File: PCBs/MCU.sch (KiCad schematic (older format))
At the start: 21 parts, among them CON2 AVR-ISP-6, J10 SPK, U6 ATMEGA328P-AU, Y2 20Mhz

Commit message: ADX988 CAT: add FE, FI commands
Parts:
- added J7: Conn_01x10, Pin_Headers:Pin_Header_Straight_1x10_Pitch2.54mm, symbol Conn_01x10
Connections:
- net IO_0 is gone; now on net RX_TX: U6.23 ((PCINT8/ADC0)PC0)
- net +5V: now also J7.9 (Pin_9)
- net GND: now also J7.1 (Pin_1)
- net IO_4: now also J7.2 (Pin_2)
- net IO_5: now also J7.3 (Pin_3)
- net IO_6: now also J7.4 (Pin_4)
- net IO_7: now also J7.5 (Pin_5)
- net RX_TX: no longer U6.14 ((PCINT2/OC1B/~SS~)PB2)
- net ENCODER_A renamed IO_8
- net IO_8: now also J7.6 (Pin_6)
- net ENCODER_B renamed IO_9
- net IO_9: now also J7.7 (Pin_7)
- new net +12V: J7.10 (Pin_10)
- new net IO_10: J7.8 (Pin_8), U6.14 ((PCINT2/OC1B/~SS~)PB2)
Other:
- moved on the sheet: D3, D4, R12, R13

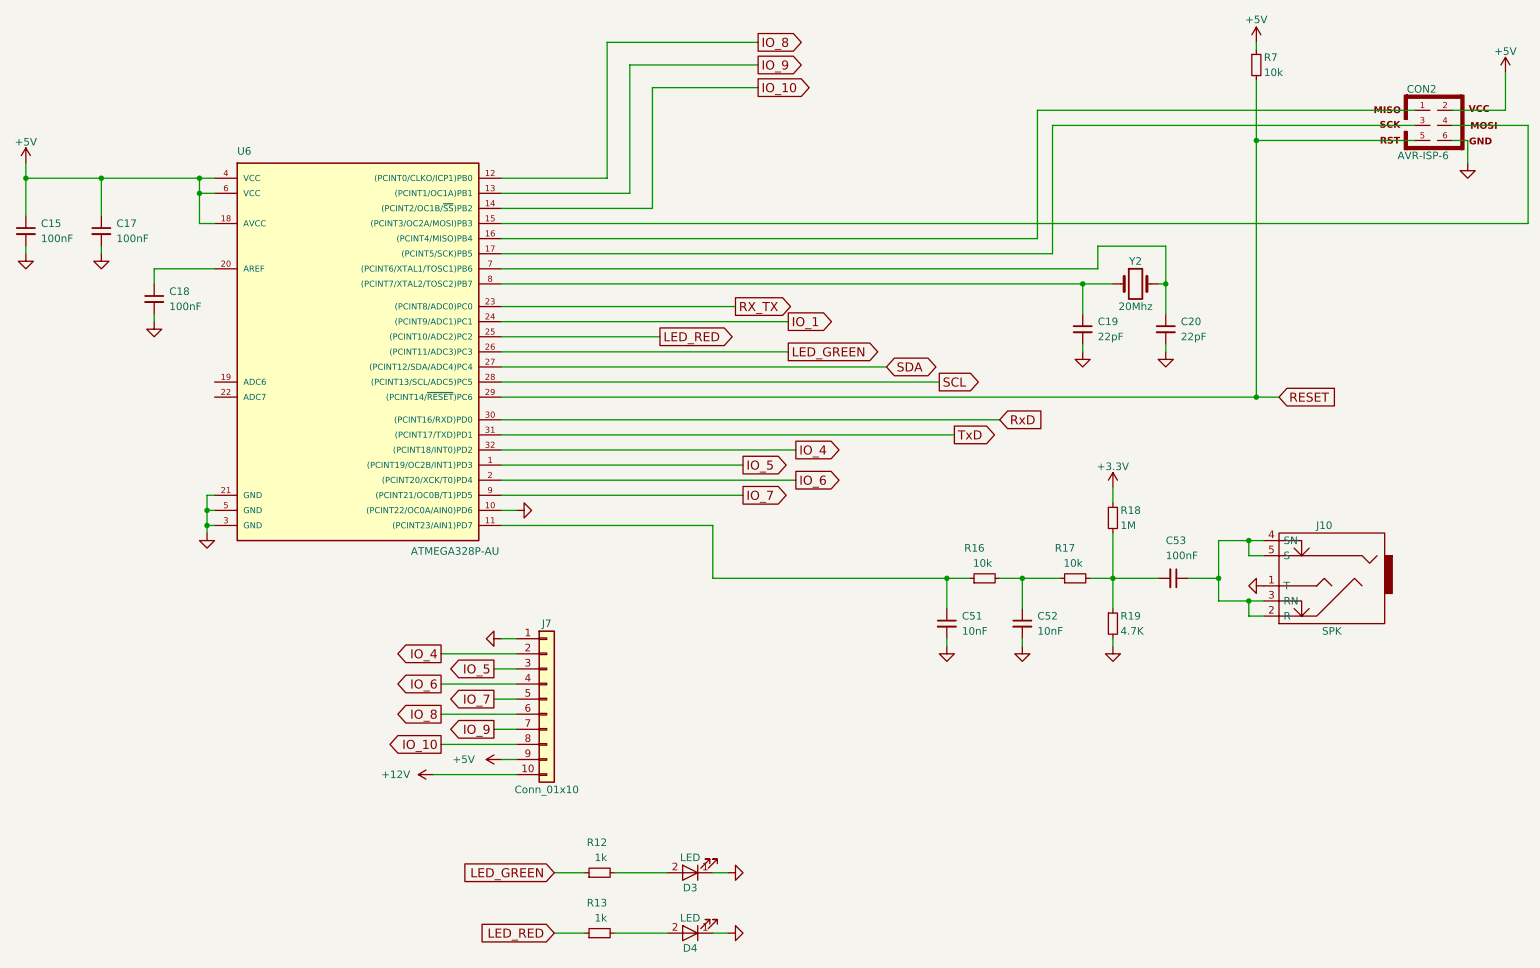
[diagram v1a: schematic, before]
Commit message: discret, simple, CH340E
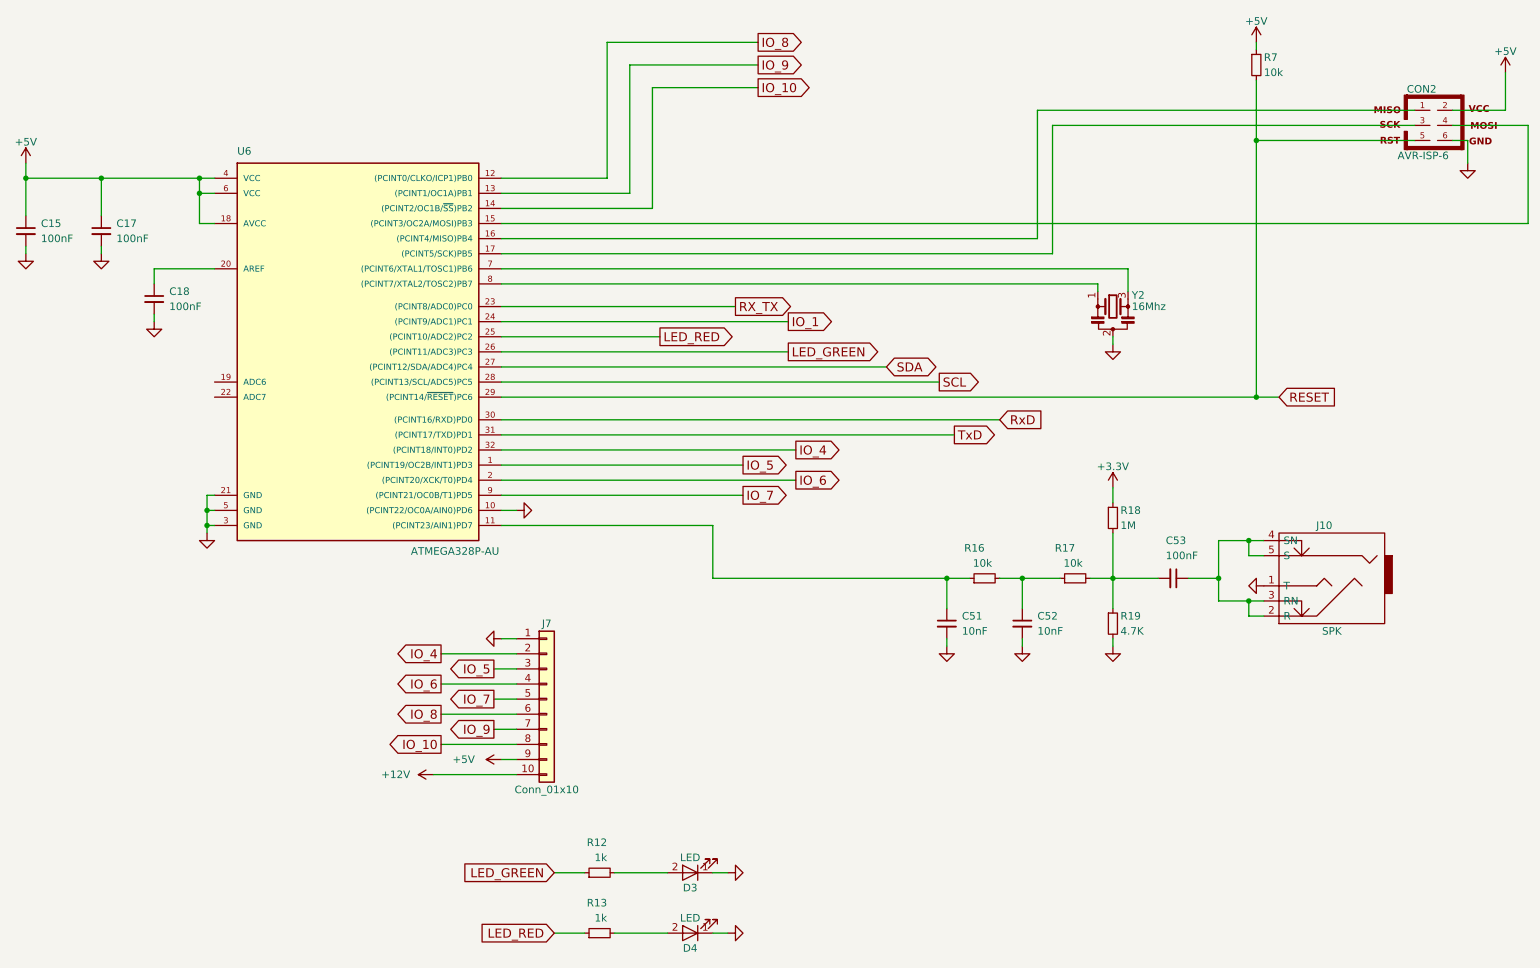
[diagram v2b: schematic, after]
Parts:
- removed C19, C20: 22pF, LCSDR:C_1206_0603, symbol C_Small
- removed Y2: 20Mhz, Crystals:Crystal_HC49-U_Vertical, symbol Crystal
- added Y2: 16Mhz, LCSDR:Crystal_SMD_3213_3.2x1.3mm, symbol Resonator_Small
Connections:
- net GND: now also Y2.2
- net at U6.7 ((PCINT6/XTAL1/TOSC1)PB6): now also Y2.3
- net at U6.8 ((PCINT7/XTAL2/TOSC2)PB7): now also Y2.1

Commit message: INIT project, si5351 generate properly frequency
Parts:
- removed C17, C18: 100nF, LCSDR:C_1206_0603, symbol C_Small
- removed CON2: AVR-ISP-6, Connectors_IDC:IDC-Header_2x03_Pitch2.54mm_Straight, symbol AVR-ISP-6
- removed R7: 10k, LCSDR:R_1206_0603, symbol R_Small
- removed U6: ATMEGA328P-AU, Housings_QFP:TQFP-32_7x7mm_Pitch0.8mm, symbol ATMEGA328P-AU
- removed Y2: 16Mhz, LCSDR:Crystal_SMD_3213_3.2x1.3mm, symbol Resonator_Small
- added C10: 100uF, Capacitors_THT:CP_Radial_D6.3mm_P2.50mm, symbol CP_Small
- added C12: 100nF, Capacitors_SMD:C_0603_HandSoldering, symbol C_Small
- added U1: 24LC01, Housings_SOIC:SOIC-8_3.9x4.9mm_Pitch1.27mm, symbol 24LC01
- added U6: Arduino_Nano, Arduino:Arduino_Nano, symbol Arduino_Nano
- C15, C51, C52: footprint LCSDR:C_1206_0603 -> Capacitors_SMD:C_0603_HandSoldering
- C53: value 100nF -> 1uF; footprint LCSDR:C_1206_0603 -> Capacitors_SMD:C_0603_HandSoldering
- D3, D4: footprint LEDs:LED_D3.0mm_Horizontal_O3.81mm_Z10.0mm -> LEDs:LED_0603_HandSoldering
- R12, R13, R16, R17, R18, R19: footprint LCSDR:R_1206_0603 -> Resistors_SMD:R_0603_HandSoldering
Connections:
- net +12V: now also U6.30 (VIN)
- net +5V: now also C10.1, C12.1, U1.8 (VCC), U6.27 (+5V)
- net GND: now also C10.2, C12.2, U1.4 (GND), U6.29 (GND), U6.4 (GND), U6.9 (~~D6)
- net IO_10: now also U6.22 (A3/D17)
- net IO_4: now also U6.13 (~~D10)
- net IO_5: now also U6.12 (~~D9)
- net IO_6: now also U6.11 (D8)
- net IO_7: now also U6.19 (A0/D14)
- net IO_8: now also U6.20 (A1/D15)
- net IO_9: now also U6.21 (A2/D16)
- net LED_GREEN: now also U6.7 (D4)
- net LED_RED: now also U6.8 (~~D5)
- net RX_TX: now also U6.5 (D2)
- net SCL: now also U1.6 (SCL), U6.24 (A5/D19)
- net SDA: now also U1.5 (SDA), U6.23 (A4/D18)
- net AUDIO_IN: now reaches C51.1, R16.1
- net AUDIO_IN: now also U6.10 (D7), U6.25 (A6/D20), U6.26 (A7/D21)
- new net RX_TX_PA: U6.6 (~~D3)
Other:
- moved on the sheet: C15, C51, C52, C53, D3, D4, J10, J7, R12, R13, R16, R17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

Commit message: add printout, finish PCB, add LM7805
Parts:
- added R7: 0, Resistors_SMD:R_0603_HandSoldering, symbol R_Small
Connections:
- net +5V: now also R7.2; no longer U6.27 (+5V)
- new net: R7.1, U6.27 (+5V)
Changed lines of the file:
@@
 $EndComp
 $Comp
-L GND #PWR025
+L GND #PWR29
 U 1 1 6253E194
 P 1300 4250
-F 0 "#PWR025" H 1300 4000 50  0001 C CNN
+F 0 "#PWR29" H 1300 4000 50  0001 C CNN
 F 1 "GND" H 1300 4100 50  0001 C CNN
 F 2 "" H 1300 4250 50  0001 C CNN
@@
 $EndComp
 $Comp
-L GND #PWR026
+L GND #PWR49
 U 1 1 630BAF4C
 P 9400 1450
-F 0 "#PWR026" H 9400 1200 50  0001 C CNN
+F 0 "#PWR49" H 9400 1200 50  0001 C CNN
 F 1 "GND" H 9400 1300 50  0001 C CNN
 F 2 "" H 9400 1450 50  0001 C CNN
@@
 $EndComp
 $Comp
-L GND #PWR027
+L GND #PWR48
 U 1 1 630BB5BE
 P 8400 1850
-F 0 "#PWR027" H 8400 1600 50  0001 C CNN
+F 0 "#PWR48" H 8400 1600 50  0001 C CNN
 F 1 "GND" H 8400 1700 50  0001 C CNN
 F 2 "" H 8400 1850 50  0001 C CNN
@@
 $EndComp
 $Comp
-L GND #PWR028
+L GND #PWR44
 U 1 1 630BBB74
 P 7800 1850
-F 0 "#PWR028" H 7800 1600 50  0001 C CNN
+F 0 "#PWR44" H 7800 1600 50  0001 C CNN
 F 1 "GND" H 7800 1700 50  0001 C CNN
 F 2 "" H 7800 1850 50  0001 C CNN
@@
 $EndComp
 $Comp
-L GND #PWR029
+L GND #PWR42
 U 1 1 630BBC47
 P 7300 1850
-F 0 "#PWR029" H 7300 1600 50  0001 C CNN
+F 0 "#PWR42" H 7300 1600 50  0001 C CNN
 F 1 "GND" H 7300 1700 50  0001 C CNN
 F 2 "" H 7300 1850 50  0001 C CNN
@@
 $EndComp
 $Comp
-L +3.3V #PWR030
+L +3.3V #PWR47
 U 1 1 630BBFA8
 P 8400 800
-F 0 "#PWR030" H 8400 650 50  0001 C CNN
+F 0 "#PWR47" H 8400 650 50  0001 C CNN
 F 1 "+3.3V" H 8400 940 50  0000 C CNN
 F 2 "" H 8400 800 50  0001 C CNN
@@
 $EndComp
 $Comp
-L GND #PWR031
+L GND #PWR40
 U 1 1 630C5E43
 P 6750 3850
-F 0 "#PWR031" H 6750 3600 50  0001 C CNN
+F 0 "#PWR40" H 6750 3600 50  0001 C CNN
 F 1 "GND" H 6750 3700 50  0001 C CNN
 F 2 "" H 6750 3850 50  0001 C CNN
@@
 $EndComp
 $Comp
-L GND #PWR032
+L GND #PWR41
 U 1 1 630C8C09
 P 6750 4250
-F 0 "#PWR032" H 6750 4000 50  0001 C CNN
+F 0 "#PWR41" H 6750 4000 50  0001 C CNN
 F 1 "GND" H 6750 4100 50  0001 C CNN
 F 2 "" H 6750 4250 50  0001 C CNN
@@
 IO_4
 $Comp
-L GND #PWR033
+L GND #PWR45
 U 1 1 63329439
 P 7850 2350
-F 0 "#PWR033" H 7850 2100 50  0001 C CNN
+F 0 "#PWR45" H 7850 2100 50  0001 C CNN
 F 1 "GND" H 7850 2200 50  0001 C CNN
 F 2 "" H 7850 2350 50  0001 C CNN
@@
 IO_10
 $Comp
-L +5V #PWR034
+L +5V #PWR46
 U 1 1 63329C42
 P 7850 3150
-F 0 "#PWR034" H 7850 3000 50  0001 C CNN
+F 0 "#PWR46" H 7850 3000 50  0001 C CNN
 F 1 "+5V" V 7850 3400 50  0000 C CNN
 F 2 "" H 7850 3150 50  0001 C CNN
@@
 $EndComp
 $Comp
-L +12V #PWR035
+L +12V #PWR43
 U 1 1 63329E6E
 P 7400 3250
-F 0 "#PWR035" H 7400 3100 50  0001 C CNN
+F 0 "#PWR43" H 7400 3100 50  0001 C CNN
 F 1 "+12V" V 7400 3500 50  0000 C CNN
 F 2 "" H 7400 3250 50  0001 C CNN
@@
 $EndComp
 $Comp
-L +5V #PWR036
+L +5V #PWR28
 U 1 1 638231F2
 P 1300 3950
-F 0 "#PWR036" H 1300 3800 50  0001 C CNN
+F 0 "#PWR28" H 1300 3800 50  0001 C CNN
 F 1 "+5V" H 1300 4090 50  0000 C CNN
 F 2 "" H 1300 3950 50  0001 C CNN
@@
 	4150 2500 4850 2500
 Wire Wire Line
-	4150 2200 4850 2200
-$Comp
-L +5V #PWR037
+	4150 2200 4700 2200
+$Comp
+L +5V #PWR38
 U 1 1 6383A51D
-P 4850 2200
-F 0 "#PWR037" H 4850 2050 50  0001 C CNN
-F 1 "+5V" V 4850 2400 50  0000 C CNN
-F 2 "" H 4850 2200 50  0001 C CNN
-F 3 "" H 4850 2200 50  0001 C CNN
-	1    4850 2200
+P 5000 2200
+F 0 "#PWR38" H 5000 2050 50  0001 C CNN
+F 1 "+5V" V 5000 2400 50  0000 C CNN
+F 2 "" H 5000 2200 50  0001 C CNN
+F 3 "" H 5000 2200 50  0001 C CNN
+	1    5000 2200
 	0    1    1    0
 $EndComp
@@
 AUDIO_IN
 $Comp
-L GND #PWR038
+L GND #PWR33
 U 1 1 6383B0B5
 P 2900 2700
-F 0 "#PWR038" H 2900 2450 50  0001 C CNN
+F 0 "#PWR33" H 2900 2450 50  0001 C CNN
 F 1 "GND" H 2900 2550 50  0001 C CNN
 F 2 "" H 2900 2700 50  0001 C CNN
@@
 	2900 2700 2950 2700
 $Comp
-L GND #PWR039
+L GND #PWR32
 U 1 1 6383B21A
 P 2900 2200
-F 0 "#PWR039" H 2900 1950 50  0001 C CNN
+F 0 "#PWR32" H 2900 1950 50  0001 C CNN
 F 1 "GND" H 2900 2050 50  0001 C CNN
 F 2 "" H 2900 2200 50  0001 C CNN
@@
 	2900 2200 2950 2200
 $Comp
-L GND #PWR040
+L GND #PWR34
 U 1 1 6383B3AA
 P 4200 2000
-F 0 "#PWR040" H 4200 1750 50  0001 C CNN
+F 0 "#PWR34" H 4200 1750 50  0001 C CNN
 F 1 "GND" H 4200 1850 50  0001 C CNN
 F 2 "" H 4200 2000 50  0001 C CNN
@@
 LED_GREEN
 $Comp
-L +12V #PWR041
+L +12V #PWR35
 U 1 1 6383B913
 P 4300 1900
-F 0 "#PWR041" H 4300 1750 50  0001 C CNN
+F 0 "#PWR35" H 4300 1750 50  0001 C CNN
 F 1 "+12V" V 4300 2150 50  0000 C CNN
 F 2 "" H 4300 1900 50  0001 C CNN
@@
 $EndComp
 $Comp
-L GND #PWR042
+L GND #PWR31
 U 1 1 6383C121
 P 2300 4650
-F 0 "#PWR042" H 2300 4400 50  0001 C CNN
+F 0 "#PWR31" H 2300 4400 50  0001 C CNN
 F 1 "GND" H 2300 4500 50  0001 C CNN
 F 2 "" H 2300 4650 50  0001 C CNN
@@
 	2700 4300 3400 4300
 $Comp
-L +5V #PWR043
+L +5V #PWR30
 U 1 1 6383C532
 P 2300 3950
-F 0 "#PWR043" H 2300 3800 50  0001 C CNN
+F 0 "#PWR30" H 2300 3800 50  0001 C CNN
 F 1 "+5V" H 2250 4100 50  0000 C CNN
 F 2 "" H 2300 3950 50  0001 C CNN
@@
 $EndComp
 $Comp
-L GND #PWR044
+L GND #PWR39
 U 1 1 63842115
 P 5450 1200
-F 0 "#PWR044" H 5450 950 50  0001 C CNN
+F 0 "#PWR39" H 5450 950 50  0001 C CNN
 F 1 "GND" H 5450 1050 50  0001 C CNN
 F 2 "" H 5450 1200 50  0001 C CNN
@@
 $EndComp
 $Comp
-L GND #PWR045
+L GND #PWR37
 U 1 1 6384211B
 P 4950 1200
-F 0 "#PWR045" H 4950 950 50  0001 C CNN
+F 0 "#PWR37" H 4950 950 50  0001 C CNN
 F 1 "GND" H 4950 1050 50  0001 C CNN
 F 2 "" H 4950 1200 50  0001 C CNN
@@
 Connection ~ 4950 900
 $Comp
-L +5V #PWR046
+L +5V #PWR36
 U 1 1 63842129
 P 4850 900
-F 0 "#PWR046" H 4850 750 50  0001 C CNN
+F 0 "#PWR36" H 4850 750 50  0001 C CNN
 F 1 "+5V" V 4850 1100 50  0000 C CNN
 F 2 "" H 4850 900 50  0001 C CNN
@@
 Wire Wire Line
 	4850 900  5450 900
+$Comp
+L R_Small R7
+U 1 1 639E7B69
+P 4800 2200
+F 0 "R7" V 5000 2200 50  0000 L CNN
+F 1 "0" V 4900 2250 50  0000 L CNN
+F 2 "Resistors_SMD:R_0603_HandSoldering" H 4800 2200 50  0001 C CNN
+F 3 "" H 4800 2200 50  0001 C CNN
+	1    4800 2200
+	0    -1   -1   0
+$EndComp
+Wire Wire Line
+	4900 2200 5000 2200
 $EndSCHEMATC
